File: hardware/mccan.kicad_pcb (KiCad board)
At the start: 8 copper layers, 200 x 140 mm, 238 parts, among them J1 PWR pigtail -> SS1.5 3w, J2 Prog/UART, J3 FL pigtail -> SS1.0 key A / b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, J4 FR pigtail -> SS1.0 key B / g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, J5 RL pigtail -> SS1.0 key C / b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, J6 RR pigtail -> SS1.0 key D / n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, J7 DENALI pigtail -> SS1.5 3w, J8 CAN pigtail -> SS1.0 2w, Q10 IPT008N06NM5LF, Q11 IPT008N06NM5LF, Q12 MMBT3904, Q2 MMBT3904, Q3 MMBT3904, Q4 NX5020UNBKS, Q5 NX5020UNBKS, Q6 NX5020UNBKS, Q7 NX5020UNBKS, Q8 NX5020UNBKS, Q9 NX5020UNBKS, SW1 BOOT, SW2 EN/RESET, U1 LM5164DDA, U10 LTC4380HMS-2, U2 LM5164DDA, U3 LM51571-Q1, U4 DML3017LDC, U5 ESP32-WROOM-32E-N8, U6 TJA1042T/3, U7 PCA9685PW/Q900, U8 ADG706, U9 BTS7008-2EPA

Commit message: hw(pcb): In4.Cu is a solid VBAT plane; the rail islands orphaned pads
spec 3.2 split In4.Cu four ways because +24V, +5V and VLOGIC_IN are POWER-class
2.0 mm tracks and a zone costs no routing effort. Measured on this placement it
does not work. rail_island() is a bounding box over every pad of a net, and all
three nets span the board: /+24V's eleven pads run x 83.38..174.58, so its island
is 98.4 x 20.0 mm and swallows five /VBAT pads -- C18.1, C19.1, C45.1, L3.1 and
R16.1, the boost input caps and the boost inductor. Every rail also holds pads of
the other two. All three sat at priority 1, so which net owned the contested copper
was order-dependent, and under any ordering the loser's pads get no plane copper.

A rail zone only replaces routing if it is continuous, so it must span its own pads,
so it must cross what lies between them. Crossing GND and the signal nets is free.
Crossing another rail orphans it, and crossing VBAT's taps starves the feed.

So In4.Cu is VBAT alone and the rails go back to being routed -- 11, 7 and 6 pads,
where the 2.0 mm width was the objection and never the count. route_external's
HANDS_OFF drops the POWER class so the external router picks them up.

Also: check_vias.touches_pad tested a via as a square and over-reported by up to
0.124 mm at a pad corner, failing the build on a drop via 0.0393 mm clear of U4.6.
It is the exact circle test now, which is what gen_pcb already uses to place them.

Co-Authored-By: Claude Sonnet 5 <noreply@anthropic.com>
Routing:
- removed copper zone on In4.Cu, net /+24V
- removed copper zone on In4.Cu, net /+5V
- removed copper zone on In4.Cu, net /VLOGIC_IN
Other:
- board text added: "1 oz) -- see scripts/check_plane_width.py. On F.Cu the FEED class floor is"
- board text added: "106.50 mm on its worst cut against the 11.44 mm IPC-2221 asks (10 C rise, internal,"
- board text added: "F.Cu sig / In1.Cu GND / In2.Cu sig (CAN pair) / In3.Cu GND / In4.Cu POWER (VBAT) /"
- board text added: "FEED path (7.0 A cont, 7.8 A transient): the In4.Cu polygon is a solid /VBAT plane,"
- board text added: "other net (see route_external.HANDS_OFF), not carved out as zones. Measured at"
- board text added: "priority 0, nothing else on the layer -- +24V, +5V and VLOGIC_IN are routed like any"
- board text removed: "F.Cu sig / In1.Cu GND / In2.Cu sig (CAN pair) / In3.Cu GND / In4.Cu POWER (split) /"
- board text removed: "FEED path (7.0 A cont, 7.8 A transient): the In4.Cu polygon, /VBAT at priority 0 with"
- board text removed: "against the 11.44 mm IPC-2221 asks (10 C rise, internal, 1 oz) -- see"
- board text removed: "gen_pcb.rail_island) -- not a hand-drawn split. Measured at 106.50 mm on its worst cut"
- board text removed: "scripts/check_plane_width.py. On F.Cu the FEED class floor is"
- board text removed: "the +24V / +5V / +VLOGIC_IN rails carved out as pad-bounded islands at priority 1 (see"
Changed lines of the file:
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@@
 		(effects (font (size 1.5 1.5) (thickness 0.225)) (justify left))
 	)
-	(gr_text "F.Cu sig / In1.Cu GND / In2.Cu sig (CAN pair) / In3.Cu GND / In4.Cu POWER (split) /" (at 23 130.3) (layer "Cmts.User")
+	(gr_text "F.Cu sig / In1.Cu GND / In2.Cu sig (CAN pair) / In3.Cu GND / In4.Cu POWER (VBAT) /" (at 23 130.3) (layer "Cmts.User")
 		(effects (font (size 1.5 1.5) (thickness 0.225)) (justify left))
 	)
@@
 		(effects (font (size 1.5 1.5) (thickness 0.225)) (justify left))
 	)
-	(gr_text "FEED path (7.0 A cont, 7.8 A transient): the In4.Cu polygon, /VBAT at priority 0 with" (at 23 138.7) (layer "Cmts.User")
+	(gr_text "FEED path (7.0 A cont, 7.8 A transient): the In4.Cu polygon is a solid /VBAT plane," (at 23 138.7) (layer "Cmts.User")
 		(effects (font (size 1.5 1.5) (thickness 0.225)) (justify left))
 	)
-	(gr_text "the +24V / +5V / +VLOGIC_IN rails carved out as pad-bounded islands at priority 1 (see" (at 23 140.8) (layer "Cmts.User")
+	(gr_text "priority 0, nothing else on the layer -- +24V, +5V and VLOGIC_IN are routed like any" (at 23 140.8) (layer "Cmts.User")
 		(effects (font (size 1.5 1.5) (thickness 0.225)) (justify left))
 	)
-	(gr_text "gen_pcb.rail_island) -- not a hand-drawn split. Measured at 106.50 mm on its worst cut" (at 23 142.9) (layer "Cmts.User")
+	(gr_text "other net (see route_external.HANDS_OFF), not carved out as zones. Measured at" (at 23 142.9) (layer "Cmts.User")
 		(effects (font (size 1.5 1.5) (thickness 0.225)) (justify left))
 	)
-	(gr_text "against the 11.44 mm IPC-2221 asks (10 C rise, internal, 1 oz) -- see" (at 23 145) (layer "Cmts.User")
+	(gr_text "106.50 mm on its worst cut against the 11.44 mm IPC-2221 asks (10 C rise, internal," (at 23 145) (layer "Cmts.User")
 		(effects (font (size 1.5 1.5) (thickness 0.225)) (justify left))
 	)
-	(gr_text "scripts/check_plane_width.py. On F.Cu the FEED class floor is" (at 23 147.1) (layer "Cmts.User")
+	(gr_text "1 oz) -- see scripts/check_plane_width.py. On F.Cu the FEED class floor is" (at 23 147.1) (layer "Cmts.User")
 		(effects (font (size 1.5 1.5) (thickness 0.225)) (justify left))
 	)
@@
 			)
 		)
-	)
-	(zone (net 4) (net_name "/+24V") (layer "In4.Cu")
-		(name "24V_IN4") (hatch edge 0.5) (priority 1)
-		(connect_pads thru_hole_only (clearance 0.3))
-		(min_thickness 0.3) (filled_areas_thickness no)
-		(fill yes (thermal_gap 0.4) (thermal_bridge_width 0.5))
-		(polygon
-			(pts
-				(xy 79.8 19.2)
-				(xy 178.205 19.2)
-				(xy 178.205 39.205)
-				(xy 79.8 39.205)
-			)
-		)
-	)
-	(zone (net 3) (net_name "/+5V") (layer "In4.Cu")
-		(name "5V_IN4") (hatch edge 0.5) (priority 1)
-		(connect_pads thru_hole_only (clearance 0.3))
-		(min_thickness 0.3) (filled_areas_thickness no)
-		(fill yes (thermal_gap 0.4) (thermal_bridge_width 0.5))
-		(polygon
-			(pts
-				(xy 80.955 29.235)
-				(xy 199.855 29.235)
-				(xy 199.855 91.905)
-				(xy 80.955 91.905)
-			)
-		)
-	)
-	(zone (net 23) (net_name "/VLOGIC_IN") (layer "In4.Cu")
-		(name "VLOGIC_IN4") (hatch edge 0.5) (priority 1)
-		(connect_pads thru_hole_only (clearance 0.3))
-		(min_thickness 0.3) (filled_areas_thickness no)
-		(fill yes (thermal_gap 0.4) (thermal_bridge_width 0.5))
-		(polygon
-			(pts
-				(xy 55.45 21.05)
-				(xy 115.1 21.05)
-				(xy 115.1 87.405)
-				(xy 55.45 87.405)
-			)
-		)

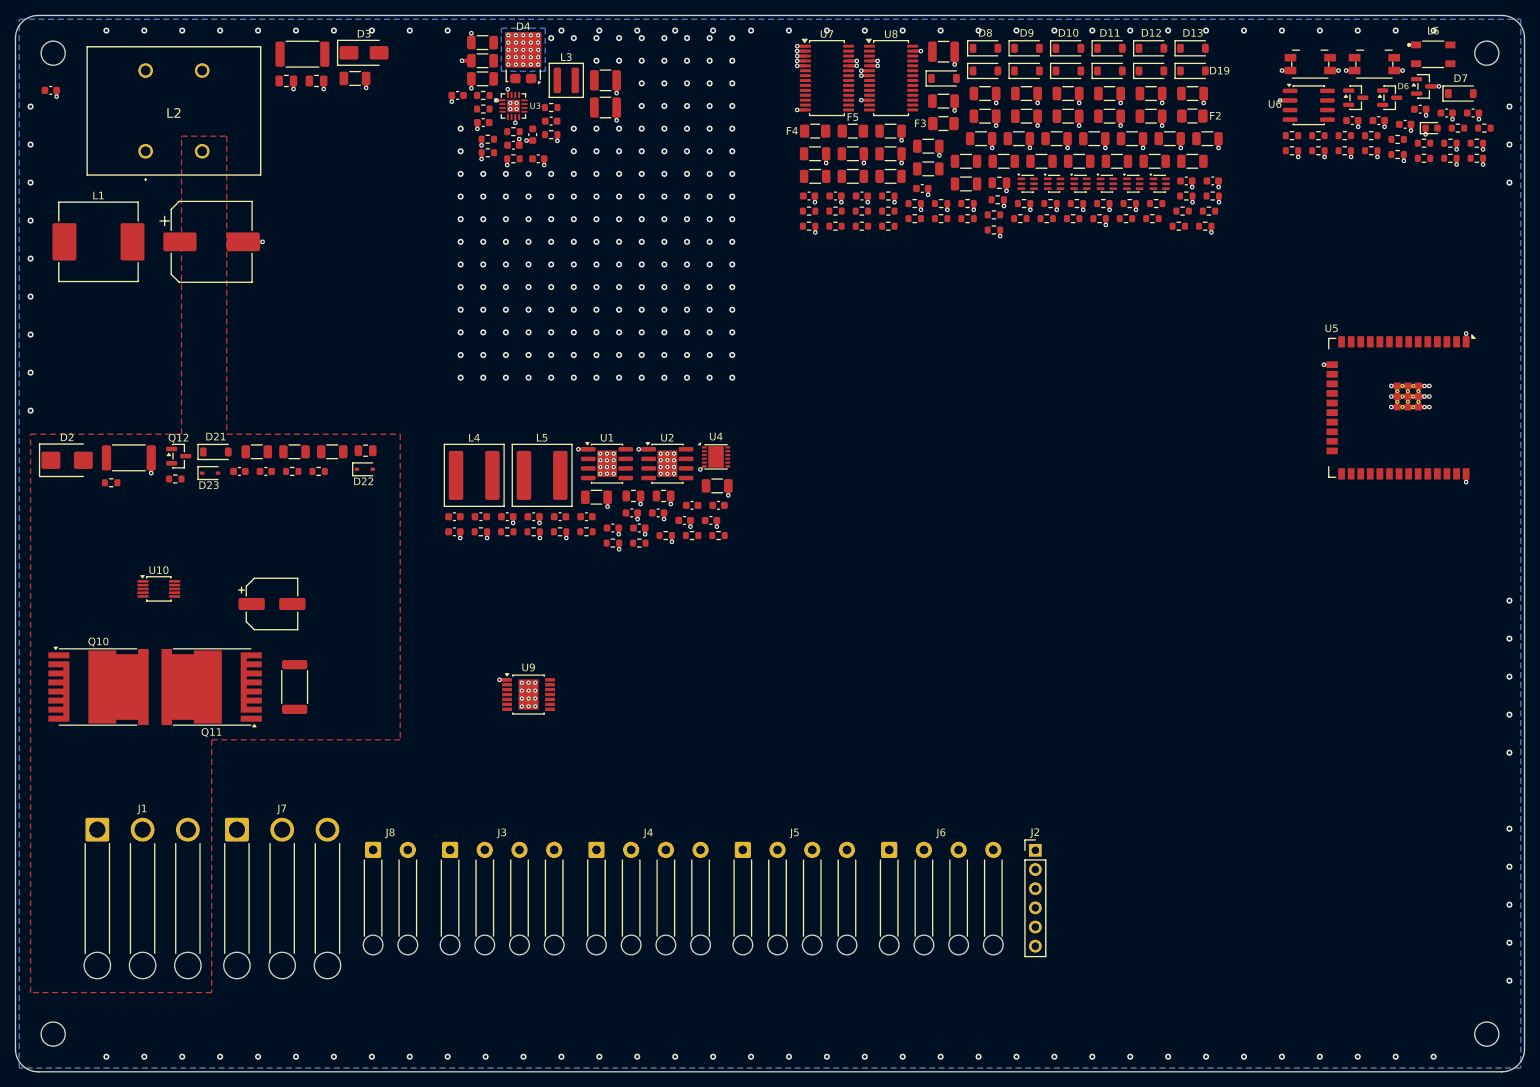
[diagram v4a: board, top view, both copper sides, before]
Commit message: hw(pcb): a designator with nowhere to go fails the build
silk_refs() used to try the library position, then four sides, then shrink to the
board minimum, then demote to F.Fab. That ladder turns a placement failure into a
board that cannot be read on the bench, silently -- twelve parts on the six-layer
board had no reference designator at all.

Both fallbacks are gone. If a designator cannot be printed legibly at full size next
to its own part, that is the placer's problem and the build stops.

Turning it on named 17 parts, so the placer had to answer them:

GUT, the gutter between auto-flowed courtyards, goes 0.4 -> 1.2 mm. 0.4 was the
six-layer board's value, chosen when area was scarce; on 200 x 140 it was buying
nothing and costing every designator in the driver field its room. At 1.2 the
auto-flow re-packs and 16 of the 17 come back.

The seventeenth was U3, and no gutter fixes it: U3 is placed, not flowed, and the
boost commutation loop around it is tight on purpose -- D4, R14, R15/R16 and R12 all
sit inside 1.4 mm of an edge. The candidate ladder only ever tried the four axis
midpoints, so a part hemmed in on all four axes had nowhere to go. It now tries the
four diagonals at each push as well, and reaches 2.8 mm. A corner is still full-size
text beside its own part; the axis midpoint was never the requirement.

_font_set() and SILK_REF_MIN_H/_T go with the shrink block -- nothing else used them.

silk references: 54 left alone, 7 moved. All six gates exit 0; DRC reports 0
violations, 0 schematic-parity issues and 0 silkscreen items.

Co-Authored-By: Claude Opus 5 <noreply@anthropic.com>
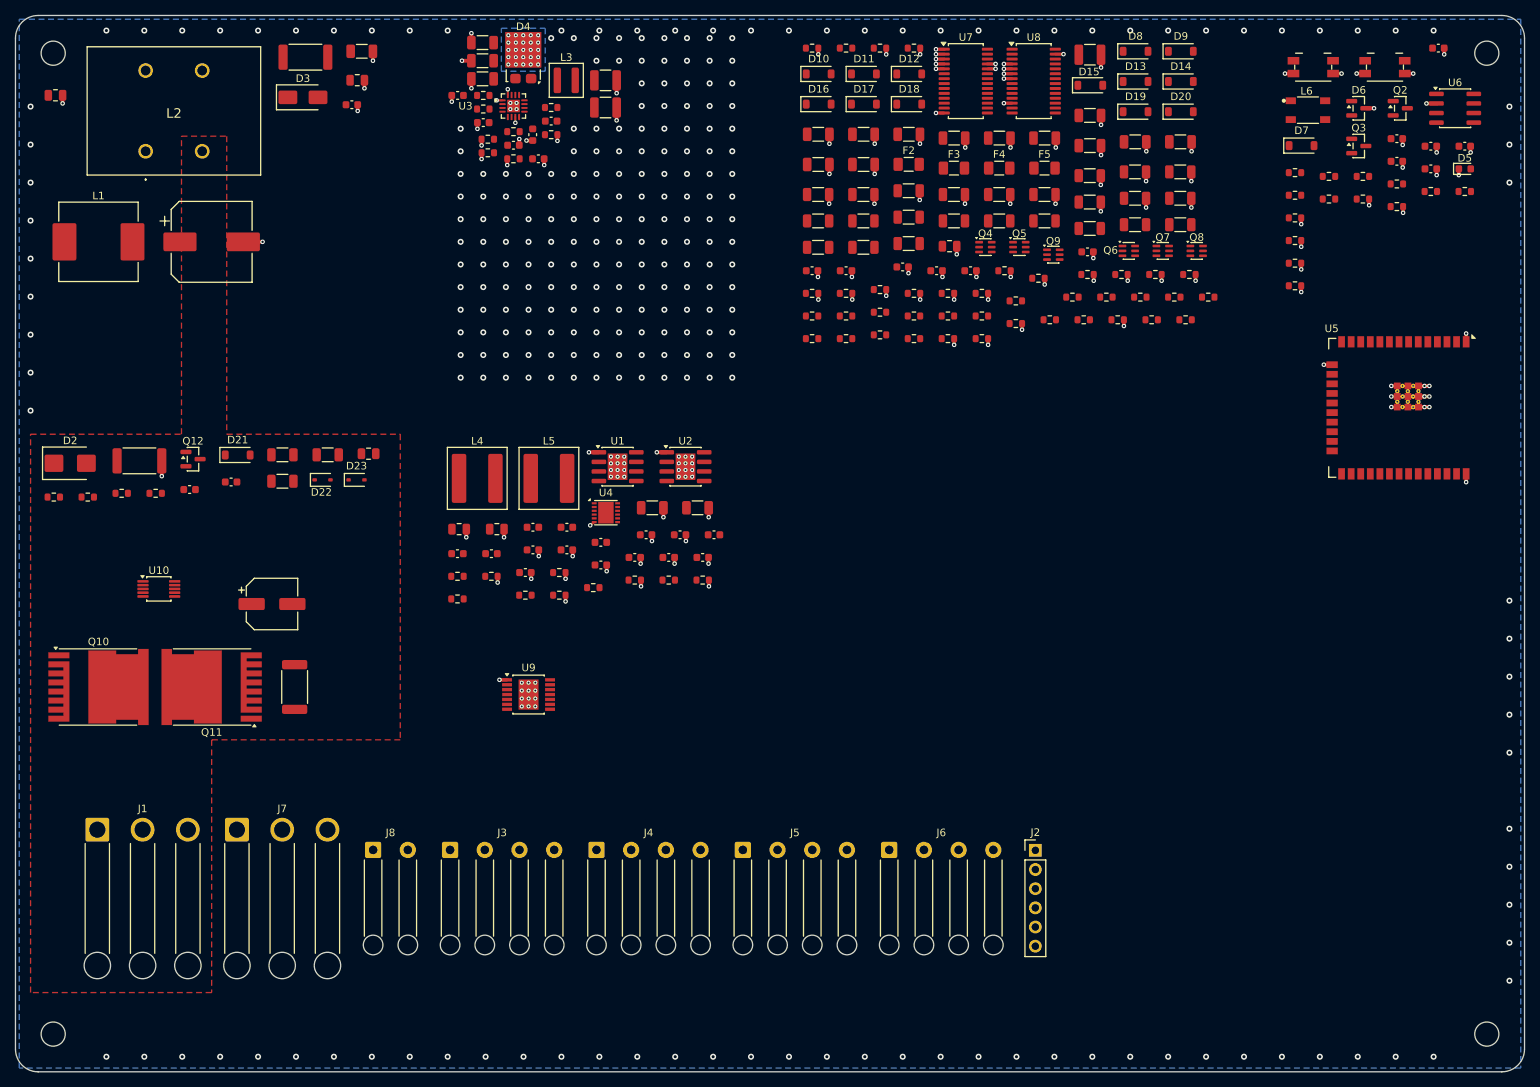
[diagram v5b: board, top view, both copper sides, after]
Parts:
- moved R36 78.9 mm to (125.6, 24.3)
- moved R37 78.0 mm to (130.1, 24.3)
- moved R38 77.0 mm to (134.6, 24.3)
- moved R39 76.0 mm to (139.1, 24.3)
- moved R70 45.6 mm to (134.6, 59.3)
- moved R68 43.9 mm to (178.1, 57.3)
- moved R62 43.8 mm to (174.4, 44.2)
- moved R67 42.9 mm to (173.6, 57.3)
- moved R61 42.8 mm to (168.4, 44.2)
- moved C42 42.7 mm to (137.6, 53.3)
- moved R66 42.0 mm to (169.1, 57.3)
- moved R65 41.0 mm to (164.6, 57.3)
- moved C1 39.9 mm to (64.6, 31.8)
- moved C59 39.1 mm to (126.4, 39.8)
- moved C60 38.6 mm to (132.4, 39.8)
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
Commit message: hw(pcb): the 7 A feed, poured through the left band
One direction only -- J1 up through the eFuse, up through L2 and the pi filter, out
of the top of input. Nothing doubles back. Poured rather than tracked: the FEED
class's 3.5 mm is a 20 K-rise floor for hops of a few mm, and every real run here is
>= 4.5 mm or is on the In4.Cu plane.

Co-Authored-By: Claude Sonnet 5 <noreply@anthropic.com>
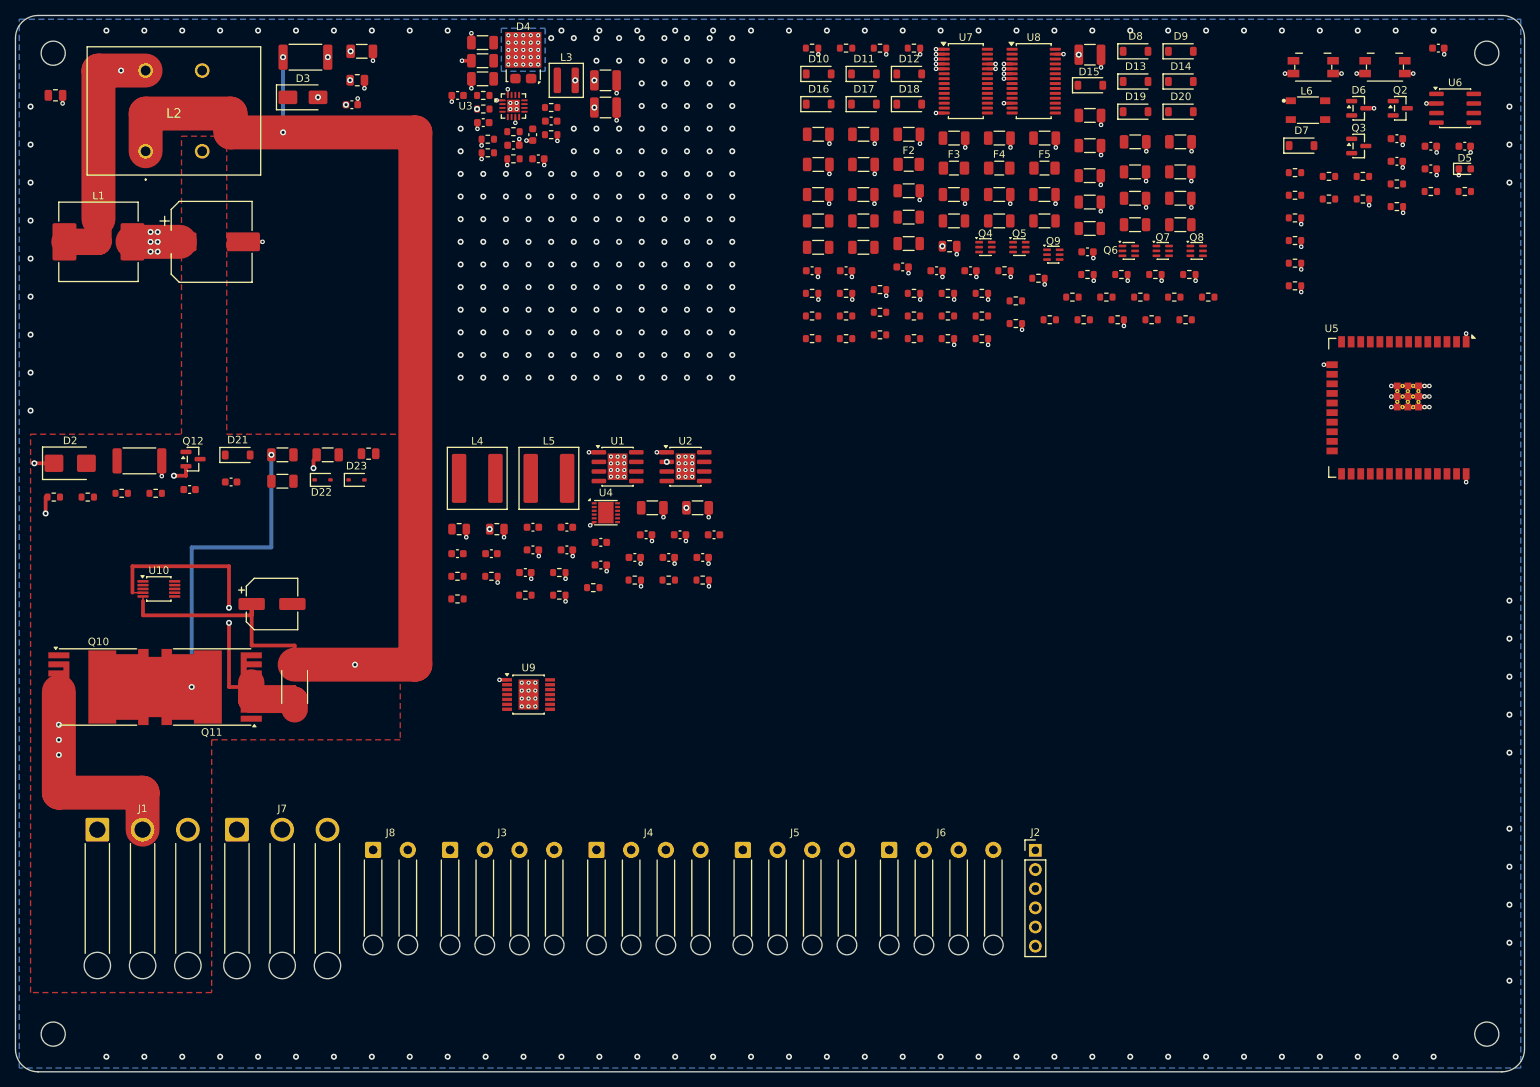
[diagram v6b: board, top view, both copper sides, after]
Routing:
- net /power_input/VBAT_PROT: track 0.00 -> 273.6 mm, vias 0 -> 4
- net /power_input/FEED_P: track 0.00 -> 188.3 mm, vias 0 -> 6
- net /power_input/VBAT_F: track 0.00 -> 75.3 mm, vias 0 -> 3
- net /power_input/SNS: track 0.00 -> 54.7 mm, vias 0 -> 2
- net /power_input/MID: track 0.00 -> 44.7 mm, vias 0 -> 2
- net /VBAT: track 0.00 -> 6.29 mm, vias 12 -> 30

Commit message: hw(pcb): the feed's narrow stretch was 7.5 mm, and a riser split a pour
Two fixes from the Task 7 review, both verified by ablation rather than argument.

The VBAT_F trunk carried the full 7.0 A over 7.5 mm at 3.5 mm under a comment claiming
"the last 3 mm". The end-cap conflict it was dodging is real -- turning at x=31.0 leaves
0.0085 mm to the VBAT link's cap against a 0.3 mm floor -- but the answer was to move the
turn, not thin the copper. At x=30.5 the same 4.5 mm track clears by 0.5085 mm and the
trunk is 4.5 mm end to end. VBAT_F never reaches a plane (In4.Cu is /VBAT, a different
net), so every millimetre of it is the only copper there is.

GNDIN_F was filling as two islands and DRC called it zero violations, because a split
fill is an unconnected item. pcbnew's own ZONE_FILLER found the orphan at
x=[36.050,47.749] y=[93.550,98.950]; all four walls are hand-track clearance offsets,
and U10's pads close the fifth side. VBAT_PROT pin 5's F.Cu riser was one of only two
hand-routed walls, so it goes to In5.Cu on two vias. Restoring it to F.Cu brings the
island straight back; with it moved, the filler reports one island spanning the zone.

The reviewer's alternative for U10's Kelvin escape was tried and is worse: a 0.8/0.4
via's 0.4 mm radius needs more clearance from SNS's crossbar than the 0.2 mm track it
replaces, so y=97.2 fails gen_pcb's own check at 0.200 < 0.300. The escape stays, with
the measurement in the comment.

Gates all 0. DRC 0 violations, 0 parity, 320 unconnected (321 before). No GND_IN line
anywhere in the report.

Co-Authored-By: Claude Opus 5 <noreply@anthropic.com>
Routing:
- net /power_input/VBAT_PROT: vias 4 -> 6
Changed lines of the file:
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@@
 	(segment
 		(start 37.25 27.3)
-		(end 31 27.3)
+		(end 30.5 27.3)
 		(width 4.5)
 		(layer "F.Cu")
@@
 	)
 	(segment
-		(start 31 27.3)
-		(end 31 47)
+		(start 30.5 27.3)
+		(end 30.5 50)
 		(width 4.5)
 		(layer "F.Cu")
@@
 	)
 	(segment
-		(start 31 47)
-		(end 31 50)
-		(width 3.5)
-		(layer "F.Cu")
-		(net 97)
-	)
-	(segment
-		(start 31 50)
+		(start 30.5 50)
 		(end 26.4915 50)
-		(width 3.5)
+		(width 4.5)
 		(layer "F.Cu")
 		(net 97)
@@
 		(end 36.9 99.5)
 		(width 0.5)
-		(layer "F.Cu")
+		(layer "In5.Cu")
 		(net 98)
 	)
@@
 	)
 	(via
+		(at 36.9 97.6)
+		(size 0.8)
+		(drill 0.4)
+		(layers "F.Cu" "B.Cu")
+		(net 98)
+	)
+	(via
+		(at 36.9 99.5)
+		(size 0.8)
+		(drill 0.4)
+		(layers "F.Cu" "B.Cu")
+		(net 98)
+	)
+	(via
